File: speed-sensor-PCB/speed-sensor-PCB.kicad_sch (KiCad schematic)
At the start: 8 parts, among them IC1 AS5600-ASOT, J1 Conn_01x03_Pin

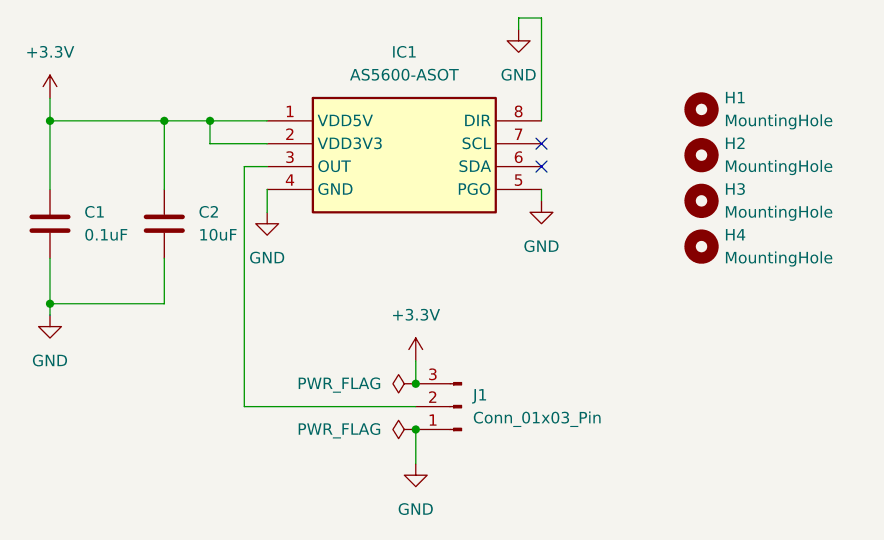
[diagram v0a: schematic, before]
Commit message: working on program, fixed PGO connection on speed detector PCB
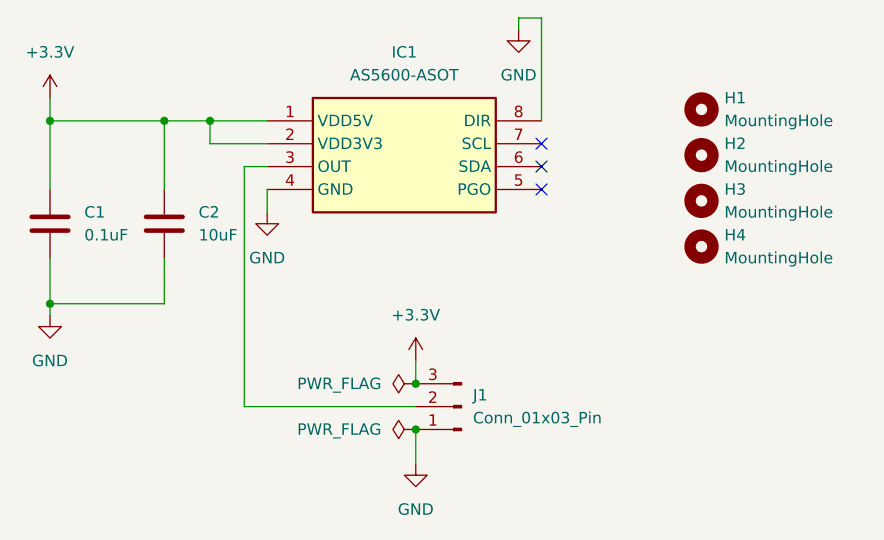
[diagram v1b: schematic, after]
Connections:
- net GND: no longer IC1.5 (PGO)
- no-connect marks 2 -> 3
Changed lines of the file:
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@@
+	)
+	(no_connect
+		(at 90.17 64.77)
 	)
 	(no_connect
@@
 		(pts
 			(xy 59.69 64.77) (xy 59.69 67.31)
-		)
-		(stroke
-			(width 0)
-			(type default)
-		)
-	)
-	(wire
-		(pts
-			(xy 90.17 66.04) (xy 90.17 64.77)
 		)
 		(stroke
@@
 					(unit 1)
 				)
-			)
-		)
-	)
-	(symbol
-		(lib_id "power:GND")
-		(at 90.17 66.04 0)
-		(unit 1)
-		(exclude_from_sim no)
-		(in_bom yes)
-		(on_board yes)
-		(dnp no)
-		(fields_autoplaced yes)
-		(property "Reference" "#PWR05"
-			(at 90.17 72.39 0)
-			(effects
-				(font
-					(size 1.27 1.27)
-				)
-				(hide yes)
-			)
-		)
-		(property "Value" "GND"
-			(at 90.17 71.12 0)
-			(effects
-				(font
-					(size 1.27 1.27)
-				)
-			)
-		)
-		(property "Footprint" ""
-			(at 90.17 66.04 0)
-			(effects
-				(font
-					(size 1.27 1.27)
-				)
-				(hide yes)
-			)
-		)
-		(property "Datasheet" ""
-			(at 90.17 66.04 0)
-			(effects
-				(font
-					(size 1.27 1.27)
-				)
-				(hide yes)
-			)
-		)
-		(property "Description" "Power symbol creates a global label with name \"GND\" , ground"
-			(at 90.17 66.04 0)
-			(effects
-				(font
-					(size 1.27 1.27)
-				)
-				(hide yes)
-			)
-		)
-		(pin "1"
-		)
-		(instances
-			(project "speed-sensor-PCB"
-				(path "/794d29e3-fe64-4cc2-bad2-bb2c3f72b9a3"
-					(reference "#PWR05")
-					(unit 1)
-				)
